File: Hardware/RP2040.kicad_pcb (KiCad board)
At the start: 2 copper layers, 34 x 34 mm, 43 parts, among them J2 Conn_01x04_Male, J3 Conn_01x02_Male, J4 Conn_01x02_Male, J5 Conn_01x02_Male, J6 Conn_01x02_Male, J7 Conn_01x08_Male, J9 QWIIC_Stackable, U1 RP2040, U2 W25Q32JVXGIQ, Y1 12MHz

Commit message: Tarduino!!!!!!!!!!!!!!!!!!!!!
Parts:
- Y1: footprint Crystal:Crystal_SMD_2016-4Pin_2.0x1.6mm -> Tinker:Crystal_SMD_2016-4Pin_2.0x1.6mm
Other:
- board text added: "????"
- board text added: "MISO"
- board text added: "MOSI"
- board text added: "RST->"
- board text added: "SCLK"
- board text added: "~{SCS}"
- board text removed: "(02)"
- board text removed: "(04)"
- board text removed: "(05)"
- board text removed: "(12)"
- board text removed: "(13)"
- board text removed: "(14)"
- board text removed: "(15)"
- board text removed: "(16)"

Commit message: whole bunche cleanup...
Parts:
- moved REF** 2.06 mm to (109.0, 87.0)
- moved G*** 2.00 mm to (91.0, 86.0)
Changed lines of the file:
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@@
   )
   (footprint "Tinker:DagNabbit" (layer "F.Cu")
-    (at 107 86.5)
+    (at 109 87)
     (attr smd board_only)
     (fp_text reference "REF**" (at 0 -8.08 unlocked) (layer "F.SilkS") hide
@@
   )
   (footprint "Tinker:NerdMage" (layer "F.Cu")
-    (at 93 85.9)
+    (at 91 86)
     (attr board_only exclude_from_pos_files exclude_from_bom)
     (fp_text reference "G***" (at 5.08 0) (layer "F.SilkS") hide

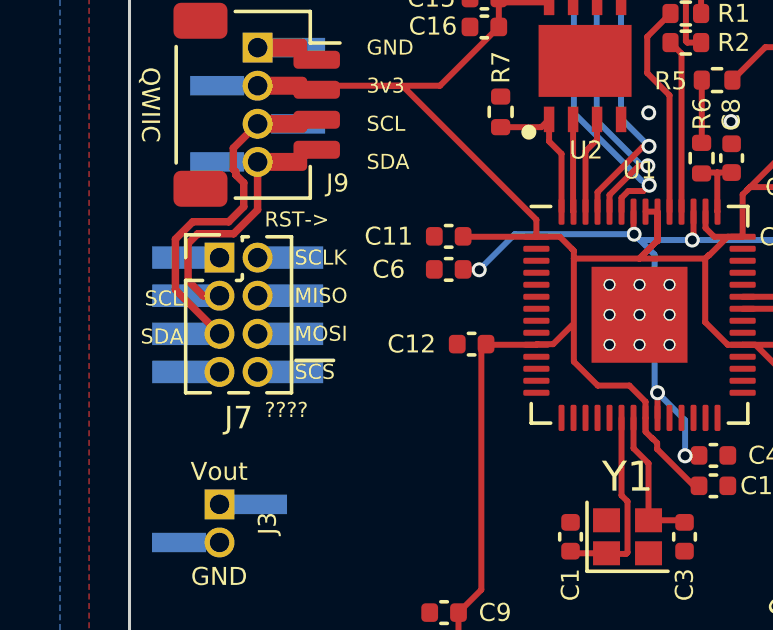
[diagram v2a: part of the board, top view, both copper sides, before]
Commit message: Still cleaning up J7
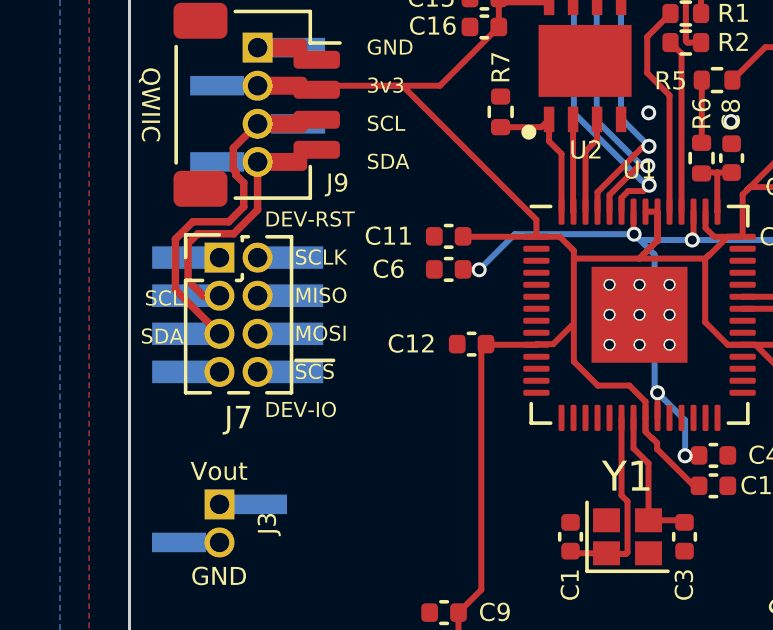
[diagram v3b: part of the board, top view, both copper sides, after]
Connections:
- net ALERT renamed DEV_GPIO
- net ATTACH renamed SCLK
- net IO12 renamed MISO
- net IO13 renamed MOSI
- net IO15 renamed ~{SCS}
- net IO16 renamed DEV_RST
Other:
- board text added: "DEV-IO"
- board text added: "DEV-RST"
- board text removed: "????"
- board text removed: "RST->"
